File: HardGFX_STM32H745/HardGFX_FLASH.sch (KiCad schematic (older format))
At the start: 3 parts, among them U6 MT25TL01GBBB8ESF-0AAT

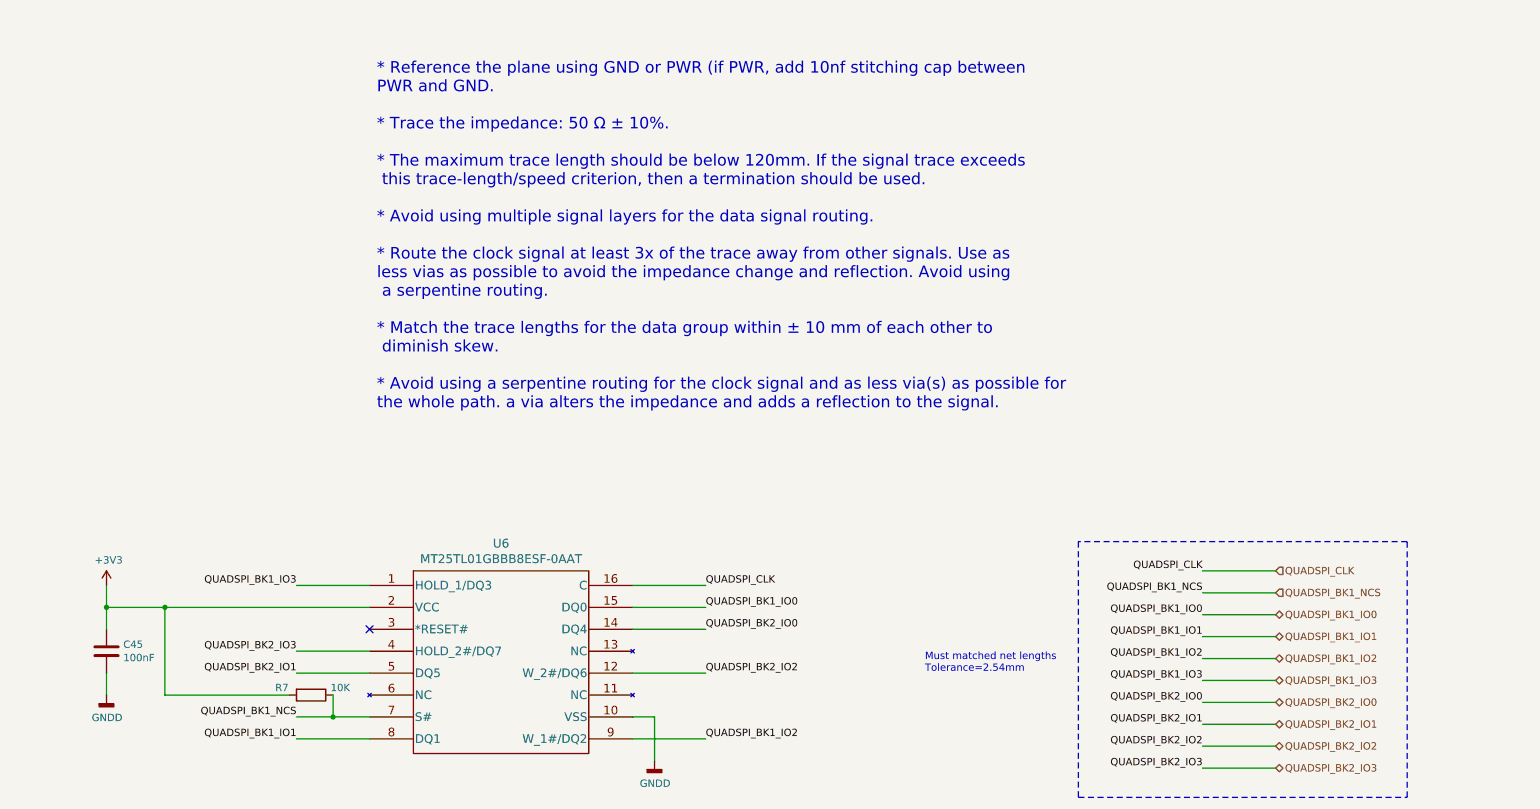
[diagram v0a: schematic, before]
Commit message: Filling field for do BOM with Kicost  and create proyect on IDE to start setting peripheral in MCU
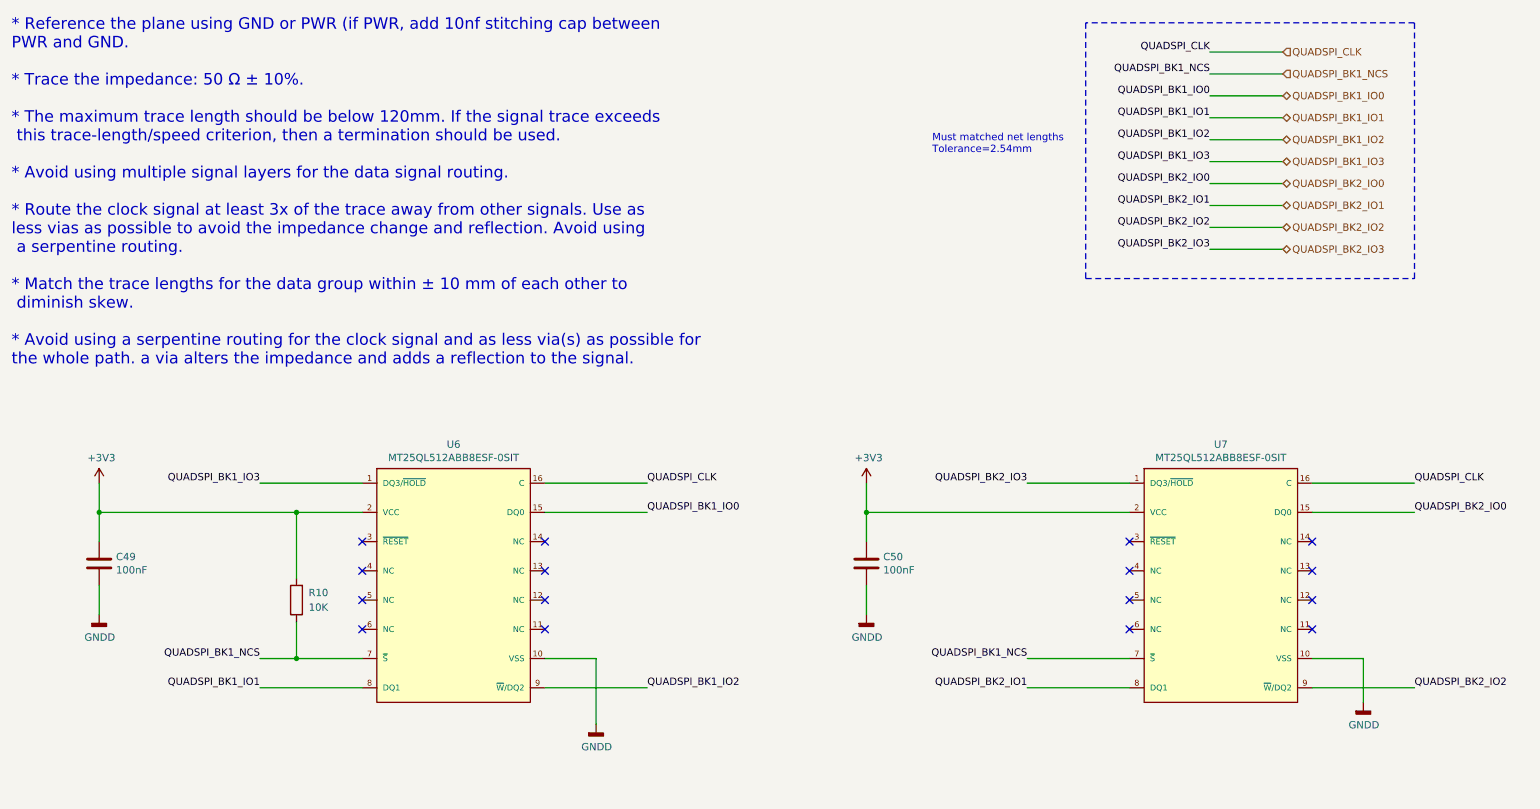
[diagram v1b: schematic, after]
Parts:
- removed U6: MT25TL01GBBB8ESF-0AAT, MT25TL01GBBB8ESF0AAT:MT25TL01GBBB8ESF-0AAT, symbol MT25TL01GBBB8ESF0AAT:MT25TL01GBBB8ESF-0AAT
- added C50: 100nF, Capacitor_SMD:C_0603_1608Metric, symbol Device:C
- added U6, U7: MT25QL512ABB8ESF-0SIT, MT25QL512ABB8ESF-0SIT:MT25QL512ABB8ESF-0SIT, symbol MT25QL512ABB8ESF-0SIT:MT25QL512ABB8ESF-0SIT
- renumbered C45 to C49, R7 to R10
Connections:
- net +3V3: now also C50.1, U6.2 (VCC), U7.2 (VCC)
- net GNDD: now also C50.2, U6.10 (VSS), U7.10 (VSS)
- net QUADSPI_BK1_IO0: now also U6.15 (DQ0)
- net QUADSPI_BK1_IO1: now also U6.8 (DQ1)
- net QUADSPI_BK1_IO2: now also U6.9 (~W~/DQ2)
- net QUADSPI_BK1_IO3: now also U6.1 (DQ3/~HOLD~)
- net QUADSPI_BK1_NCS: now also U6.7 (~S~), U7.7 (~S~)
- net QUADSPI_BK2_IO0: now also U7.15 (DQ0)
- net QUADSPI_BK2_IO1: now also U7.8 (DQ1)
- net QUADSPI_BK2_IO2: now also U7.9 (~W~/DQ2)
- net QUADSPI_BK2_IO3: now also U7.1 (DQ3/~HOLD~)
- net QUADSPI_CLK: now also U6.16 (C), U7.16 (C)
- no-connect marks 1 -> 16
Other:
- moved on the sheet: C49, R10

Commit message: Almost I end to fill Kicost field on schematics.
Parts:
- C49, C50: Digikey# (none) -> 311-1088-1-ND; MANUFACTURER (none) -> YAGEO; Manf# (none) -> CC0603KRX7R7BB104; Mouser# (none) -> 603-CC603KRX7R7BB104
- R10: Digikey# (none) -> 311-10.0KHRCT-ND; MANUFACTURER (none) -> YAGEO; Manf# (none) -> RC0603FR-0710KL; Mouser# (none) -> 603-RC0603FR-0710KL
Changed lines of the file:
@@
 Sheet 5 8
 Title "FLASH"
-Date "2021-08-24"
+Date "2021-08-25"
 Rev "Rev. 1"
 Comp "HardGFX"
@@
 F 1 "100nF" H 1515 4355 50  0000 L CNN
 F 2 "Capacitor_SMD:C_0603_1608Metric" H 1438 4250 50  0001 C CNN
-F 3 "https://ar.mouser.com/datasheet/2/447/UPY_GPHC_X7R_6_3V_to_50V_20-1995650.pdf" H 1400 4400 50  0001 C CNN
+F 3 "https://www.yageo.com/upload/media/product/productsearch/datasheet/mlcc/UPY-GPHC_X7R_6.3V-to-50V_18.pdf" H 1400 4400 50  0001 C CNN
+F 4 "311-1088-1-ND" H 1400 4400 50  0001 C CNN "Digikey#"
+F 5 "YAGEO" H 1400 4400 50  0001 C CNN "MANUFACTURER"
+F 6 "CC0603KRX7R7BB104" H 1400 4400 50  0001 C CNN "Manf#"
+F 7 "603-CC603KRX7R7BB104" H 1400 4400 50  0001 C CNN "Mouser#"
 	1    1400 4400
 	1    0    0    -1
@@
 F 1 "10K" H 2600 4700 50  0000 C CNN
 F 2 "" V 2680 4650 50  0001 C CNN
-F 3 "~" H 2750 4650 50  0001 C CNN
+F 3 "https://www.yageo.com/upload/media/product/productsearch/datasheet/rchip/PYu-RC_Group_51_RoHS_L_11.pdf" H 2750 4650 50  0001 C CNN
+F 4 "311-10.0KHRCT-ND" H 2750 4650 50  0001 C CNN "Digikey#"
+F 5 "YAGEO" H 2750 4650 50  0001 C CNN "MANUFACTURER"
+F 6 "RC0603FR-0710KL" H 2750 4650 50  0001 C CNN "Manf#"
+F 7 "603-RC0603FR-0710KL" H 2750 4650 50  0001 C CNN "Mouser#"
 	1    2750 4650
 	-1   0    0    1
@@
 F 1 "100nF" H 6765 4355 50  0000 L CNN
 F 2 "Capacitor_SMD:C_0603_1608Metric" H 6688 4250 50  0001 C CNN
-F 3 "https://ar.mouser.com/datasheet/2/447/UPY_GPHC_X7R_6_3V_to_50V_20-1995650.pdf" H 6650 4400 50  0001 C CNN
+F 3 "https://www.yageo.com/upload/media/product/productsearch/datasheet/mlcc/UPY-GPHC_X7R_6.3V-to-50V_18.pdf" H 6650 4400 50  0001 C CNN
+F 4 "311-1088-1-ND" H 6650 4400 50  0001 C CNN "Digikey#"
+F 5 "YAGEO" H 6650 4400 50  0001 C CNN "MANUFACTURER"
+F 6 "CC0603KRX7R7BB104" H 6650 4400 50  0001 C CNN "Manf#"
+F 7 "603-CC603KRX7R7BB104" H 6650 4400 50  0001 C CNN "Mouser#"
 	1    6650 4400
 	1    0    0    -1

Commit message: Modified symbols field to use Kicost
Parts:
- C49, C50: Manf# CC0603KRX7R7BB104 -> (none); manf# (none) -> CC0603KRX7R7BB104
- R10: Manf# RC0603FR-0710KL -> (none); manf# (none) -> RC0603FR-0710KL
- U6, U7: Manf# MT25QL512ABB8ESF-0SIT -> (none); manf# (none) -> MT25QL512ABB8ESF-0SIT
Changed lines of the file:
@@
 F 4 "311-1088-1-ND" H 1400 4400 50  0001 C CNN "Digikey#"
 F 5 "YAGEO" H 1400 4400 50  0001 C CNN "MANUFACTURER"
-F 6 "CC0603KRX7R7BB104" H 1400 4400 50  0001 C CNN "Manf#"
+F 6 "" H 1400 4400 50  0001 C CNN "Manf#"
 F 7 "603-CC603KRX7R7BB104" H 1400 4400 50  0001 C CNN "Mouser#"
+F 8 "CC0603KRX7R7BB104" H 1400 4400 50  0001 C CNN "manf#"
 	1    1400 4400
 	1    0    0    -1
@@
 F 4 "311-10.0KHRCT-ND" H 2750 4650 50  0001 C CNN "Digikey#"
 F 5 "YAGEO" H 2750 4650 50  0001 C CNN "MANUFACTURER"
-F 6 "RC0603FR-0710KL" H 2750 4650 50  0001 C CNN "Manf#"
+F 6 "" H 2750 4650 50  0001 C CNN "Manf#"
 F 7 "603-RC0603FR-0710KL" H 2750 4650 50  0001 C CNN "Mouser#"
+F 8 "RC0603FR-0710KL" H 2750 4650 50  0001 C CNN "manf#"
 	1    2750 4650
 	-1   0    0    1
@@
 F 3 "https://media-www.micron.com/-/media/client/global/documents/products/data-sheet/nor-flash/serial-nor/mt25q/die-rev-b/mt25q_qlkt_l_512_abb_0.pd" H 1500 2550 50  0001 L CNN
 F 4 "557-1651-ND" H 3100 4000 50  0001 C CNN "Digikey#"
-F 5 "MT25QL512ABB8ESF-0SIT" H 3100 4000 50  0001 C CNN "Manf#"
+F 5 "" H 3100 4000 50  0001 C CNN "Manf#"
 F 6 "340-278183-TRAY" H 3100 4000 50  0001 C CNN "Mouser#"
 F 7 "Micron" H 3100 4000 50  0001 C CNN "MANUFACTURER"
+F 8 "MT25QL512ABB8ESF-0SIT" H 3100 4000 50  0001 C CNN "manf#"
 	1    3100 4000
 	1    0    0    -1
@@
 F 3 "https://media-www.micron.com/-/media/client/global/documents/products/data-sheet/nor-flash/serial-nor/mt25q/die-rev-b/mt25q_qlkt_l_512_abb_0.pd" H 6750 2550 50  0001 L CNN
 F 4 "557-1651-ND" H 8350 4000 50  0001 C CNN "Digikey#"
-F 5 "MT25QL512ABB8ESF-0SIT" H 8350 4000 50  0001 C CNN "Manf#"
+F 5 "" H 8350 4000 50  0001 C CNN "Manf#"
 F 6 "340-278183-TRAY" H 8350 4000 50  0001 C CNN "Mouser#"
 F 7 "Micron" H 8350 4000 50  0001 C CNN "MANUFACTURER"
+F 8 "MT25QL512ABB8ESF-0SIT" H 8350 4000 50  0001 C CNN "manf#"
 	1    8350 4000
 	1    0    0    -1
@@
 F 4 "311-1088-1-ND" H 6650 4400 50  0001 C CNN "Digikey#"
 F 5 "YAGEO" H 6650 4400 50  0001 C CNN "MANUFACTURER"
-F 6 "CC0603KRX7R7BB104" H 6650 4400 50  0001 C CNN "Manf#"
+F 6 "" H 6650 4400 50  0001 C CNN "Manf#"
 F 7 "603-CC603KRX7R7BB104" H 6650 4400 50  0001 C CNN "Mouser#"
+F 8 "CC0603KRX7R7BB104" H 6650 4400 50  0001 C CNN "manf#"
 	1    6650 4400
 	1    0    0    -1
